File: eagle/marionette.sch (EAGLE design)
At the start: 224 parts, among them J17 MA02-1, J18 MA02-1, J19 MA02-1, J2 SWD, J20 MA02-1, J22 ZX62D-B-5P8, J6 MA03-2W, J8 MA04-2W, Q1 BSS84, U1 STM32F407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

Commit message: Routed SPI_2 sck and mosi to DAC chip Connected MCO1 to ULPI PHY Cleaned up some
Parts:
- removed MCO1: TEST-POINT, Tova:TEST-POINT
- removed USART2_CK, USART2_TX: TEST-POINT10MIL-TEST-POINT, Tova:TEST-POINT10MIL-TEST-POINT
- added C47: 0.1uF, 10V, rcl_custom:C-EU0603-C
- added SPI3_MOSI, SPI3_SCK: TEST-POINT10MIL-TEST-POINT, Tova:TEST-POINT10MIL-TEST-POINT
- C39: value 1uF, 10V -> 10uF, 10V
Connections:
- removed net USART2_CK: U1G$4.PD7, U6.SCLK, USART2_CK.1
- removed net USART2_TX: U1G$4.PD5, U6.DIN, USART2_TX.1
- net +3.3VDDA: now also C47.1
- net 3.3VDD: no longer U14.S0, U14.S2, U14.XO
- net GND: now also C47.2, U14.S0, U14.S2
- net MCO1: now also U14.XI; no longer MCO1.1
- net PH14: now also D21.I/O7, J14.20; no longer D21.I/O8, J14.19
- net PH15: now also D21.I/O8, J14.19; no longer D21.I/O7, J14.20
- net SDIO_CK: now also SPI3_MOSI.1, U6.DIN
- net SDIO_D2: now also SPI3_SCK.1, U6.SCLK
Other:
- note added: "*See Figure 8-1 USB3320 data sheet for application diagram"
- note removed: "*See Figure 8-2 USB3320 data sheet for application diagram"
- moved on the sheet: C1, C10, C11, C12, C13, C14, C15, C16, C17, C18, C19, C2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

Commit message: Connected PB14 to ULPI refclk MCO1 is connected to a test point again cleaned up GPIO routing
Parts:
- added MCO1: TEST-POINT10MIL-TEST-POINT, Tova:TEST-POINT10MIL-TEST-POINT
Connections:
- new net PD5: U1G$4.PD5
- new net PD7: LED2.C, U1G$4.PD7
- net MCO1: now also MCO1.1; no longer U14.XI
- net PB14: now also U14.XI; no longer D17.I/O8, J14.6
- net PG8: now also D17.I/O8, J14.6; no longer LED2.C
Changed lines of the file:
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@@
 <setting verticaltext="up"/>
 </settings>
-<grid distance="0.05" unitdist="inch" unit="inch" style="lines" multiple="1" display="yes" altdistance="0.01" altunitdist="inch" altunit="inch"/>
+<grid distance="0.05" unitdist="inch" unit="inch" style="lines" multiple="1" display="no" altdistance="0.01" altunitdist="inch" altunit="inch"/>
 <layers>
 <layer number="1" name="Top" color="4" fill="1" visible="no" active="no"/>
@@
 <part name="GND10" library="GROUND" deviceset="GND" device=""/>
 <part name="C47" library="rcl_custom" deviceset="C-EU" device="0603-C" value="0.1uF, 10V"/>
+<part name="MCO1" library="Tova" deviceset="TEST-POINT" device="10MIL-TEST-POINT"/>
 </parts>
 <sheets>
@@
 table 5-7 of USB3320
 data sheet</text>
+<wire x1="344.17" y1="87.63" x2="339.09" y2="87.63" width="0.1524" layer="97"/>
 </plain>
 <instances>
@@
 <attribute name="NAME" x="407.924" y="67.691" size="1.778" layer="95"/>
 </instance>
+<instance part="MCO1" gate="G$1" x="168.91" y="351.79" smashed="yes">
+<attribute name="NAME" x="167.005" y="353.695" size="1.778" layer="95" font="vector"/>
+</instance>
 </instances>
 <busses>
@@
 </segment>
 </bus>
-<bus name="GPIO_BUS:PA15,PB8,PB9,PB14,PB15,PC6,PD0,PD1,PD3,PD4,PD6,PD8,PD9,PD10,PD11,PD12,PE0,PE1,PE2,PE3,PE4,PE5,PE6,PE7,PE8,PE9,PE10,PE11,PE12,PE13,PE14,PE15,PF2,PF11,PF12,PF13,PF14,PF15,PG0,PG1,PG2,PG3,PG4,PG5,PG6,PG7,PH2,PH3,PH5,PH6,PH9,PH10,PH11,PH12,PH14,PH15,PI4,PI5,PI6,PI7,PI8,PI10,PI11">
+<bus name="GPIO_BUS:PA15,PB8,PB9,PB14,PB15,PC6,PD0,PD1,PD3,PD4,PD5,PD6,PD7,PD8,PD9,PD10,PD11,PD12,PE0,PE1,PE2,PE3,PE4,PE5,PE6,PE7,PE8,PE9,PE10,PE11,PE12,PE13,PE14,PE15,PF2,PF11,PF12,PF13,PF14,PF15,PG0,PG1,PG2,PG3,PG4,PG5,PG6,PG7,PG8,PH2,PH3,PH5,PH6,PH9,PH10,PH11,PH12,PH14,PH15,PI4,PI5,PI6,PI7,PI8,PI10,PI11">
 <segment>
 <wire x1="173.99" y1="318.77" x2="173.99" y2="50.8" width="0.762" layer="92"/>
@@
 <label x="129.54" y="227.33" size="1.778" layer="95" font="vector"/>
 </segment>
+<segment>
+<pinref part="U14" gate="U" pin="XI"/>
+<wire x1="405.13" y1="377.19" x2="405.13" y2="381" width="0.1524" layer="91"/>
+<wire x1="405.13" y1="381" x2="402.59" y2="381" width="0.1524" layer="91"/>
+<label x="402.59" y="381" size="1.778" layer="95" rot="R180" xref="yes"/>
+</segment>
 </net>
 <net name="PC15" class="0">
@@
 <segment>
 <pinref part="U1" gate="G$1" pin="PA8"/>
-<wire x1="107.95" y1="351.79" x2="170.18" y2="351.79" width="0.1524" layer="91"/>
+<wire x1="107.95" y1="351.79" x2="168.91" y2="351.79" width="0.1524" layer="91"/>
 <label x="129.54" y="351.79" size="1.778" layer="95"/>
-<label x="170.18" y="351.79" size="1.778" layer="95" xref="yes"/>
-</segment>
-<segment>
-<pinref part="U14" gate="U" pin="XI"/>
-<wire x1="405.13" y1="377.19" x2="405.13" y2="381" width="0.1524" layer="91"/>
-<wire x1="405.13" y1="381" x2="396.24" y2="381" width="0.1524" layer="91"/>
-<label x="396.24" y="381" size="1.778" layer="95" rot="R180" xref="yes"/>
+<pinref part="MCO1" gate="G$1" pin="1"/>
 </segment>
 </net>
@@
 </segment>
 </net>
+<net name="PD5" class="0">
+<segment>
+<wire x1="173.99" y1="87.63" x2="171.45" y2="85.09" width="0.1524" layer="91"/>
+<pinref part="U1" gate="G$4" pin="PD5"/>
+<wire x1="171.45" y1="85.09" x2="107.95" y2="85.09" width="0.1524" layer="91"/>
+</segment>
+</net>
+<net name="PD7" class="0">
+<segment>
+<wire x1="173.99" y1="77.47" x2="171.45" y2="74.93" width="0.1524" layer="91"/>
+<pinref part="U1" gate="G$4" pin="PD7"/>
+<wire x1="171.45" y1="74.93" x2="107.95" y2="74.93" width="0.1524" layer="91"/>
+</segment>
+</net>
 </nets>
 </sheet>
@@
 </segment>
 </bus>
-<bus name="GPIO_BUS:PA15,PB8,PB9,PB14,PB15,PC6,PD0,PD1,PD3,PD4,PD6,PD8,PD9,PD10,PD11,PD12,PE0,PE1,PE2,PE3,PE4,PE5,PE6,PE7,PE8,PE9,PE10,PE11,PE12,PE13,PE14,PE15,PF2,PF11,PF12,PF13,PF14,PF15,PG0,PG1,PG2,PG3,PG4,PG5,PG6,PG7,PH2,PH3,PH5,PH6,PH9,PH10,PH11,PH12,PH14,PH15,PI4,PI5,PI6,PI7,PI8,PI10,PI11">
+<bus name="GPIO_BUS:PA15,PB8,PB9,PB14,PB15,PC6,PD0,PD1,PD3,PD4,PD5,PD6,PD7,PD8,PD9,PD10,PD11,PD12,PE0,PE1,PE2,PE3,PE4,PE5,PE6,PE7,PE8,PE9,PE10,PE11,PE12,PE13,PE14,PE15,PF2,PF11,PF12,PF13,PF14,PF15,PG0,PG1,PG2,PG3,PG4,PG5,PG6,PG7,PG8,PH2,PH3,PH5,PH6,PH9,PH10,PH11,PH12,PH14,PH15,PI4,PI5,PI6,PI7,PI8,PI10,PI11">
 <segment>
 <wire x1="219.71" y1="257.81" x2="199.39" y2="241.3" width="0.762" layer="92"/>
@@
 </segment>
 <segment>
-<wire x1="445.77" y1="201.93" x2="445.77" y2="347.98" width="0.762" layer="92"/>
+<wire x1="445.77" y1="194.31" x2="445.77" y2="347.98" width="0.762" layer="92"/>
 <wire x1="445.77" y1="347.98" x2="443.23" y2="350.52" width="0.762" layer="92"/>
 <label x="450.85" y="267.97" size="2.54" layer="95" font="vector" rot="R90"/>
@@
 </segment>
 </net>
-<net name="PG8" class="0">
-<segment>
-<pinref part="U1" gate="G$7" pin="PG8"/>
-<wire x1="476.25" y1="195.58" x2="403.86" y2="195.58" width="0.1524" layer="91"/>
-<label x="419.1" y="195.58" size="1.778" layer="95" font="vector"/>
-<pinref part="LED2" gate="G$1" pin="C"/>
-</segment>
-</net>
 <net name="PG9" class="0">
 <segment>
@@
 </segment>
 </net>
+<net name="PG8" class="0">
+<segment>
+<wire x1="445.77" y1="198.12" x2="443.23" y2="195.58" width="0.1524" layer="91"/>
+<pinref part="U1" gate="G$7" pin="PG8"/>
+<wire x1="443.23" y1="195.58" x2="403.86" y2="195.58" width="0.1524" layer="91"/>
+<label x="419.1" y="195.58" size="1.778" layer="95"/>
+</segment>
+</net>
+<net name="PD7" class="0">
+<segment>
+<pinref part="LED2" gate="G$1" pin="C"/>
+<wire x1="476.25" y1="195.58" x2="458.47" y2="195.58" width="0.1524" layer="91"/>
+<label x="458.47" y="195.58" size="1.778" layer="95" rot="R180" xref="yes"/>
+</segment>
+</net>
 </nets>
 </sheet>
@@
 </instances>
 <busses>
-<bus name="GPIO_BUS:PA15,PB8,PB9,PB14,PB15,PC6,PD0,PD1,PD3,PD4,PD6,PD8,PD9,PD10,PD11,PD12,PE0,PE1,PE2,PE3,PE4,PE5,PE6,PE7,PE8,PE9,PE10,PE11,PE12,PE13,PE14,PE15,PF2,PF11,PF12,PF13,PF14,PF15,PG0,PG1,PG2,PG3,PG4,PG5,PG6,PG7,PH2,PH3,PH5,PH6,PH9,PH10,PH11,PH12,PH14,PH15,PI4,PI5,PI6,PI7,PI8,PI10,PI11">
+<bus name="GPIO_BUS:PA15,PB8,PB9,PB14,PB15,PC6,PD0,PD1,PD3,PD4,PD5,PD6,PD7,PD8,PD9,PD10,PD11,PD12,PE0,PE1,PE2,PE3,PE4,PE5,PE6,PE7,PE8,PE9,PE10,PE11,PE12,PE13,PE14,PE15,PF2,PF11,PF12,PF13,PF14,PF15,PG0,PG1,PG2,PG3,PG4,PG5,PG6,PG7,PG8,PH2,PH3,PH5,PH6,PH9,PH10,PH11,PH12,PH14,PH15,PI4,PI5,PI6,PI7,PI8,PI10,PI11">
 <segment>
 <wire x1="15.24" y1="220.98" x2="15.24" y2="250.19" width="0.762" layer="92"/>
@@
 </segment>
 </net>
-<net name="PB14" class="0">
-<segment>
-<wire x1="219.71" y1="242.57" x2="217.17" y2="240.03" width="0.1524" layer="91"/>
-<pinref part="J14" gate="G$1" pin="6"/>
-<wire x1="217.17" y1="240.03" x2="182.88" y2="240.03" width="0.1524" layer="91"/>
-<label x="207.01" y="240.03" size="1.778" layer="95"/>
-<wire x1="182.88" y1="240.03" x2="177.8" y2="240.03" width="0.1524" layer="91"/>
-<wire x1="182.88" y1="189.23" x2="182.88" y2="240.03" width="0.1524" layer="91"/>
-<junction x="182.88" y="240.03"/>
-<wire x1="182.88" y1="189.23" x2="181.61" y2="187.96" width="0.1524" layer="91"/>
-<pinref part="D17" gate="G$1" pin="I/O8"/>
-<wire x1="181.61" y1="187.96" x2="139.7" y2="187.96" width="0.1524" layer="91"/>
-</segment>
-</net>
 <net name="PB15" class="0">
 <segment>
@@
 </segment>
 </net>
+<net name="PG8" class="0">
+<segment>
+<wire x1="219.71" y1="242.57" x2="217.17" y2="240.03" width="0.1524" layer="91"/>
+<pinref part="J14" gate="G$1" pin="6"/>
+<wire x1="217.17" y1="240.03" x2="182.88" y2="240.03" width="0.1524" layer="91"/>
+<label x="207.01" y="240.03" size="1.778" layer="95"/>
+<wire x1="182.88" y1="240.03" x2="177.8" y2="240.03" width="0.1524" layer="91"/>
+<wire x1="182.88" y1="189.23" x2="182.88" y2="240.03" width="0.1524" layer="91"/>
+<junction x="182.88" y="240.03"/>
+<wire x1="182.88" y1="189.23" x2="181.61" y2="187.96" width="0.1524" layer="91"/>
+<pinref part="D17" gate="G$1" pin="I/O8"/>
+<wire x1="181.61" y1="187.96" x2="139.7" y2="187.96" width="0.1524" layer="91"/>
+</segment>
+</net>

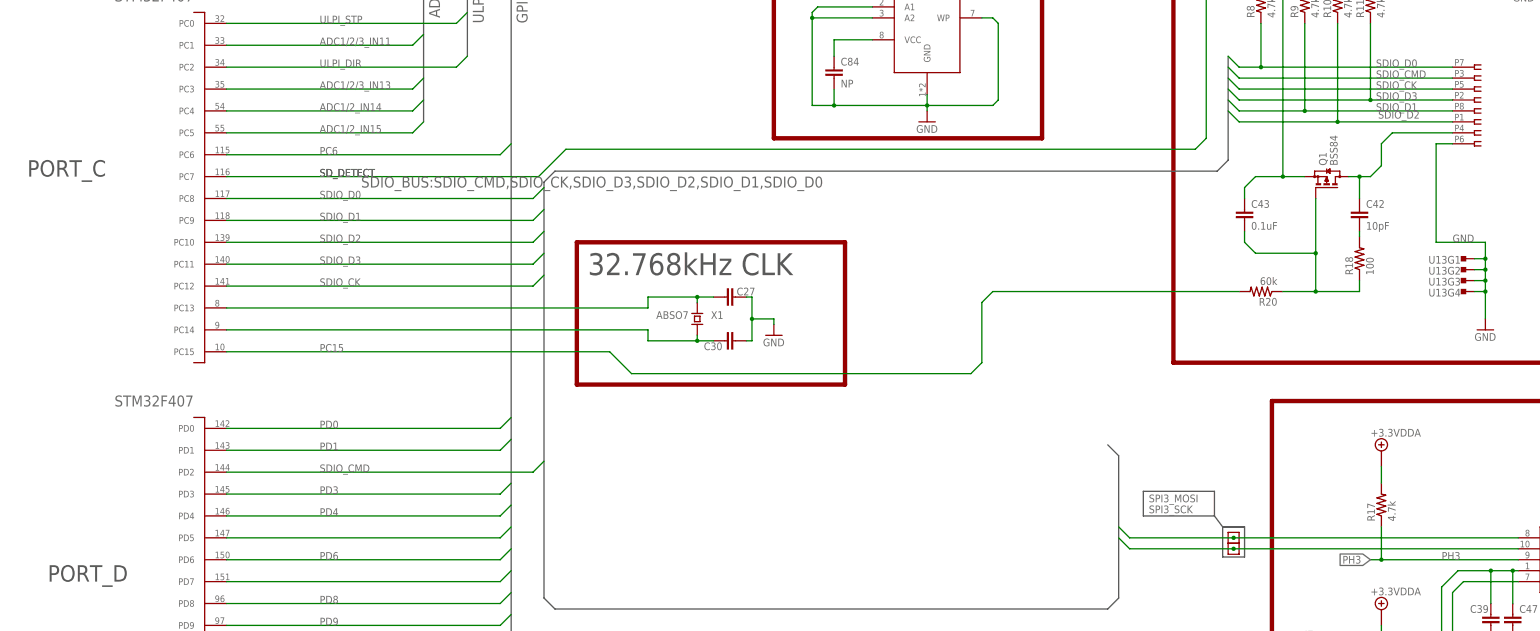
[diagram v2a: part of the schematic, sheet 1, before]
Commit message: Changed names of nets: 	SDIO_CK --> SDIO_CK-SPI3_MOSI 	SDIO_D2 --> SDIO_D2-SPI3_SCK
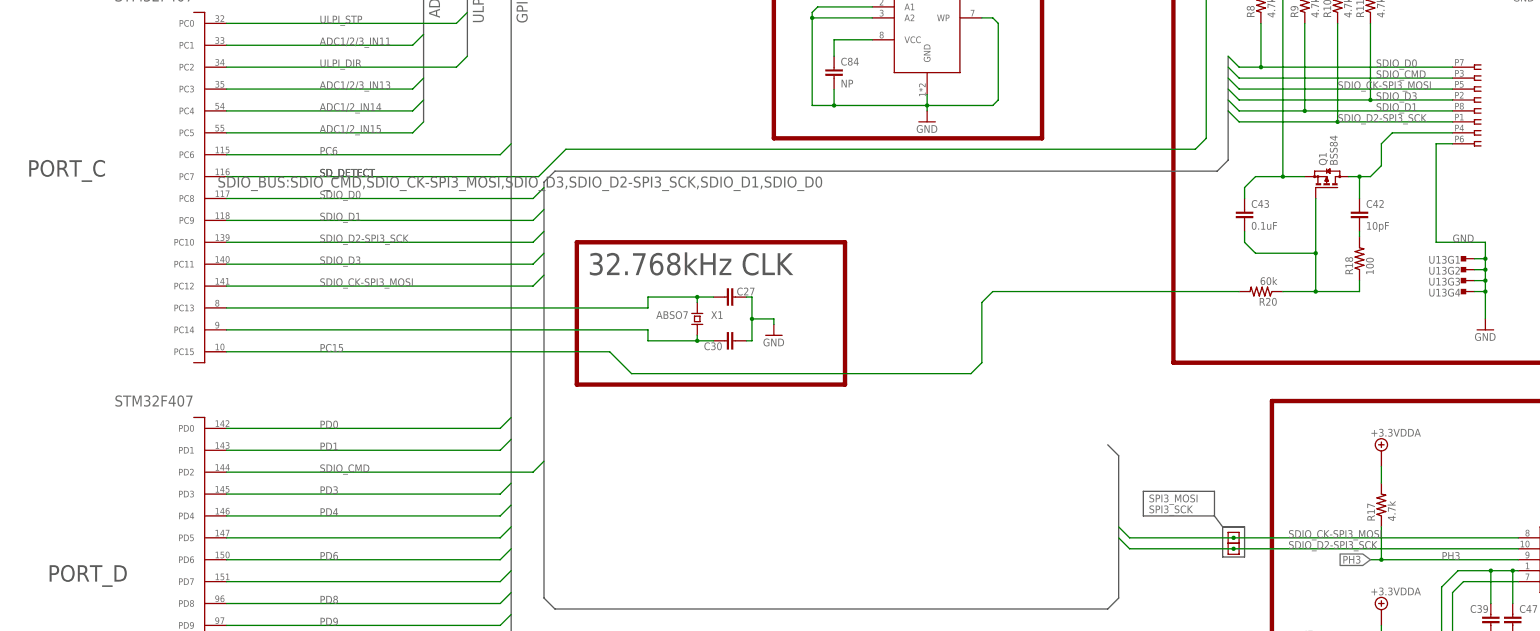
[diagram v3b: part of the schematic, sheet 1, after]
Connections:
- net SDIO_CK renamed SDIO_CK-SPI3_MOSI
- net SDIO_D2 renamed SDIO_D2-SPI3_SCK
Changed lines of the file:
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@@
 </segment>
 </bus>
-<bus name="SDIO_BUS:SDIO_CMD,SDIO_CK,SDIO_D3,SDIO_D2,SDIO_D1,SDIO_D0">
+<bus name="SDIO_BUS:SDIO_CMD,SDIO_CK-SPI3_MOSI,SDIO_D3,SDIO_D2-SPI3_SCK,SDIO_D1,SDIO_D0">
 <segment>
 <wire x1="340.36" y1="196.85" x2="340.36" y2="172.72" width="0.762" layer="92"/>
@@
 </segment>
 </net>
-<net name="SDIO_CK" class="0">
+<net name="SDIO_CK-SPI3_MOSI" class="0">
 <segment>
 <pinref part="U1" gate="G$3" pin="PC12"/>
@@
 <pinref part="U13" gate="$" pin="5"/>
 <wire x1="342.9" y1="189.23" x2="392.43" y2="189.23" width="0.1524" layer="91"/>
-<label x="374.65" y="189.23" size="1.778" layer="95" font="vector"/>
+<label x="365.76" y="189.23" size="1.778" layer="95" font="vector"/>
 </segment>
 <segment>
@@
 <wire x1="341.63" y1="85.09" x2="407.67" y2="85.09" width="0.1524" layer="91"/>
 <junction x="341.63" y="85.09"/>
+<label x="354.33" y="85.09" size="1.778" layer="95"/>
 </segment>
 </net>
@@
 </segment>
 </net>
-<net name="SDIO_D2" class="0">
+<net name="SDIO_D2-SPI3_SCK" class="0">
 <segment>
 <pinref part="U1" gate="G$3" pin="PC10"/>
@@
 <pinref part="U13" gate="$" pin="1"/>
 <wire x1="342.9" y1="181.61" x2="365.76" y2="181.61" width="0.1524" layer="91"/>
-<label x="384.81" y="184.15" size="1.778" layer="95" font="vector" rot="R180"/>
+<label x="365.76" y="181.61" size="1.778" layer="95" font="vector"/>
 <pinref part="R10" gate="R" pin="1"/>
 <wire x1="365.76" y1="181.61" x2="392.43" y2="181.61" width="0.1524" layer="91"/>
@@
 <wire x1="341.63" y1="82.55" x2="407.67" y2="82.55" width="0.1524" layer="91"/>
 <junction x="341.63" y="82.55"/>
-</segment>
-</net>
+<label x="354.33" y="82.55" size="1.778" layer="95"/>
+</segment>
+</net>

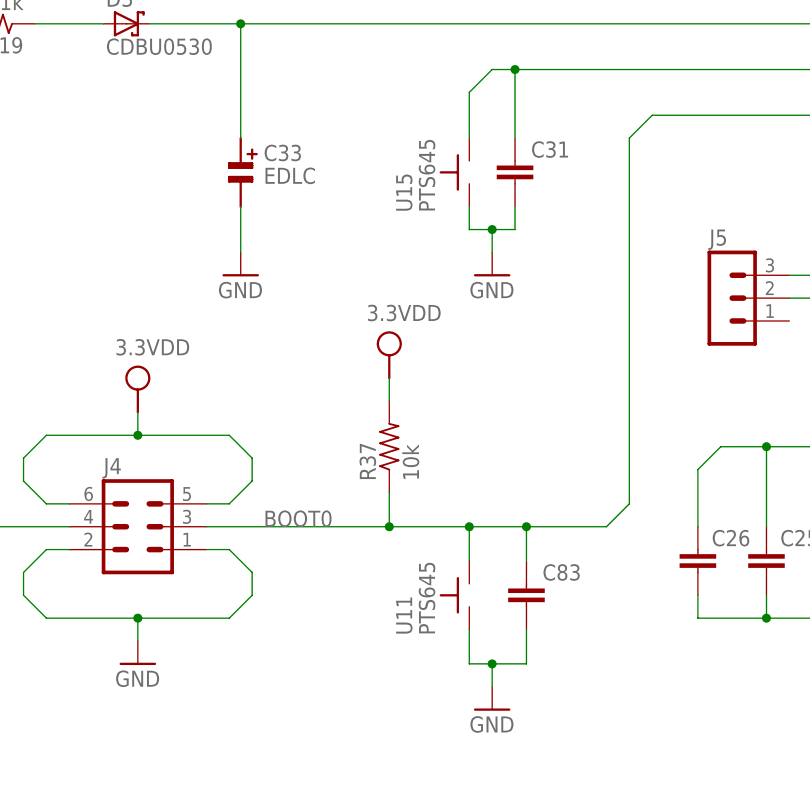
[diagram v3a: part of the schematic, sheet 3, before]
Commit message: Replaced C42 - 0603 package with 0402 package size 0603 package size is not available
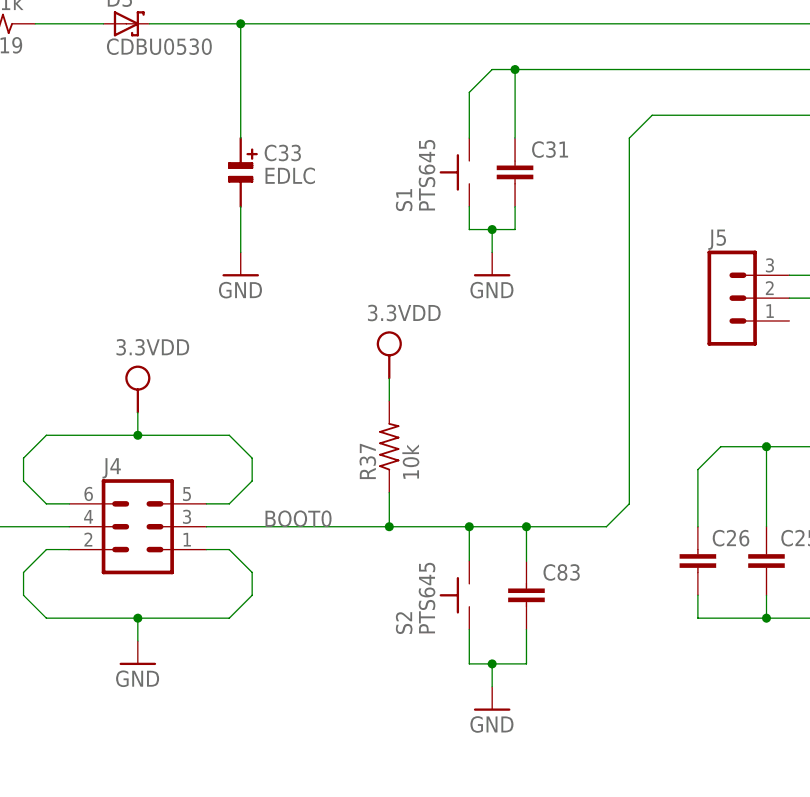
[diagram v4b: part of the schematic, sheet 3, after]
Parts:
- C42: device rcl_custom:C-EU0603-C -> rcl_custom:C-EU0402-C
- C47: value 0.1uF, 10V -> 0.1uF, 10V Low ESR
- renumbered U11 to S2, U15 to S1
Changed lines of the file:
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@@
 <setting verticaltext="up"/>
 </settings>
-<grid distance="0.05" unitdist="inch" unit="inch" style="lines" multiple="1" display="no" altdistance="0.01" altunitdist="inch" altunit="inch"/>
+<grid distance="0.1" unitdist="inch" unit="inch" style="lines" multiple="1" display="no" altdistance="0.01" altunitdist="inch" altunit="inch"/>
 <layers>
 <layer number="1" name="Top" color="4" fill="1" visible="no" active="no"/>
@@
 <part name="FRAME2" library="frames" deviceset="FRAME_C_L" device=""/>
 <part name="FRAME3" library="frames" deviceset="FRAME_B_L" device="" value="Supply"/>
-<part name="U15" library="PTS645" deviceset="PTS645" device=""/>
+<part name="S1" library="PTS645" deviceset="PTS645" device=""/>
 <part name="C31" library="rcl_custom" deviceset="C-EU" device="0603-C" value="100nF, 10V"/>
 <part name="GND9" library="GROUND" deviceset="GND" device=""/>
@@
 <part name="GND27" library="GROUND" deviceset="GND" device=""/>
 <part name="Q1" library="BSS84" deviceset="BSS84" device=""/>
-<part name="C42" library="rcl_custom" deviceset="C-EU" device="0603-C" value="10pF"/>
+<part name="C42" library="rcl_custom" deviceset="C-EU" device="0402-C" value="10pF"/>
 <part name="C43" library="rcl_custom" deviceset="C-EU" device="0603-C" value="0.1uF"/>
 <part name="R18" library="rcl_custom" deviceset="R-US_" device="0603-C" value="100"/>
@@
 <part name="GND53" library="GROUND" deviceset="GND" device=""/>
 <part name="U$39" library="3_3VDDsupply" deviceset="3.3VDD" device=""/>
-<part name="U11" library="PTS645" deviceset="PTS645" device=""/>
+<part name="S2" library="PTS645" deviceset="PTS645" device=""/>
 <part name="C83" library="rcl_custom" deviceset="C-EU" device="0603-C" value="100nF, 10V"/>
 <part name="GND54" library="GROUND" deviceset="GND" device=""/>
@@
 <part name="GND62" library="GROUND" deviceset="GND" device=""/>
 <part name="GND10" library="GROUND" deviceset="GND" device=""/>
-<part name="C47" library="rcl_custom" deviceset="C-EU" device="0603-C" value="0.1uF, 10V"/>
+<part name="C47" library="rcl_custom" deviceset="C-EU" device="0603-C" value="0.1uF, 10V Low ESR"/>
 <part name="MCO1" library="Tova" deviceset="TEST-POINT" device="10MIL-TEST-POINT"/>
 </parts>
@@
 <instance part="FRAME3" gate="G$1" x="0" y="0"/>
 <instance part="FRAME3" gate="G$2" x="325.12" y="0"/>
-<instance part="U15" gate="G$1" x="93.98" y="106.68" rot="R90"/>
+<instance part="S1" gate="G$1" x="93.98" y="106.68" rot="R90"/>
 <instance part="C31" gate="CE" x="99.06" y="107.95" smashed="yes">
 <attribute name="NAME" x="105.156" y="110.109" size="1.778" layer="95" rot="R180"/>
@@
 <attribute name="VALUE" x="173.99" y="107.95" size="1.778" layer="96"/>
 </instance>
-<instance part="U11" gate="G$1" x="93.98" y="59.69" rot="R90"/>
+<instance part="S2" gate="G$1" x="93.98" y="59.69" rot="R90"/>
 <instance part="C83" gate="CE" x="100.33" y="60.96" smashed="yes">
 <attribute name="NAME" x="106.426" y="63.119" size="1.778" layer="95" rot="R180"/>
@@
 <wire x1="96.52" y1="100.33" x2="96.52" y2="97.79" width="0.1524" layer="91"/>
 <pinref part="GND9" gate="1" pin="GND"/>
-<pinref part="U15" gate="G$1" pin="P$1"/>
+<pinref part="S1" gate="G$1" pin="P$1"/>
 <wire x1="93.98" y1="102.87" x2="93.98" y2="100.33" width="0.1524" layer="91"/>
 <pinref part="C31" gate="CE" pin="2"/>
@@
 <wire x1="100.33" y1="55.88" x2="100.33" y2="52.07" width="0.1524" layer="91"/>
 <wire x1="100.33" y1="52.07" x2="96.52" y2="52.07" width="0.1524" layer="91"/>
-<pinref part="U11" gate="G$1" pin="P$1"/>
+<pinref part="S2" gate="G$1" pin="P$1"/>
 <wire x1="96.52" y1="52.07" x2="93.98" y2="52.07" width="0.1524" layer="91"/>
 <wire x1="93.98" y1="52.07" x2="93.98" y2="55.88" width="0.1524" layer="91"/>
@@
 <wire x1="99.06" y1="118.11" x2="96.52" y2="118.11" width="0.1524" layer="91"/>
 <wire x1="96.52" y1="118.11" x2="93.98" y2="115.57" width="0.1524" layer="91"/>
-<pinref part="U15" gate="G$1" pin="P$2"/>
+<pinref part="S1" gate="G$1" pin="P$2"/>
 <wire x1="93.98" y1="115.57" x2="93.98" y2="110.49" width="0.1524" layer="91"/>
 <pinref part="C31" gate="CE" pin="1"/>
@@
 <label x="156.21" y="113.03" size="1.778" layer="95"/>
 <pinref part="J4" gate="1" pin="3"/>
-<pinref part="U11" gate="G$1" pin="P$2"/>
+<pinref part="S2" gate="G$1" pin="P$2"/>
 <wire x1="93.98" y1="63.5" x2="93.98" y2="67.31" width="0.1524" layer="91"/>
 <pinref part="C83" gate="CE" pin="1"/>
